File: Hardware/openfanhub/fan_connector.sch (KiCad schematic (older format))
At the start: 10 parts, among them M1 Fan_4pin, Q4 Q_PMOS_DGS, Q5 Q_NMOS_DGS, Q6 Q_NMOS_DGS

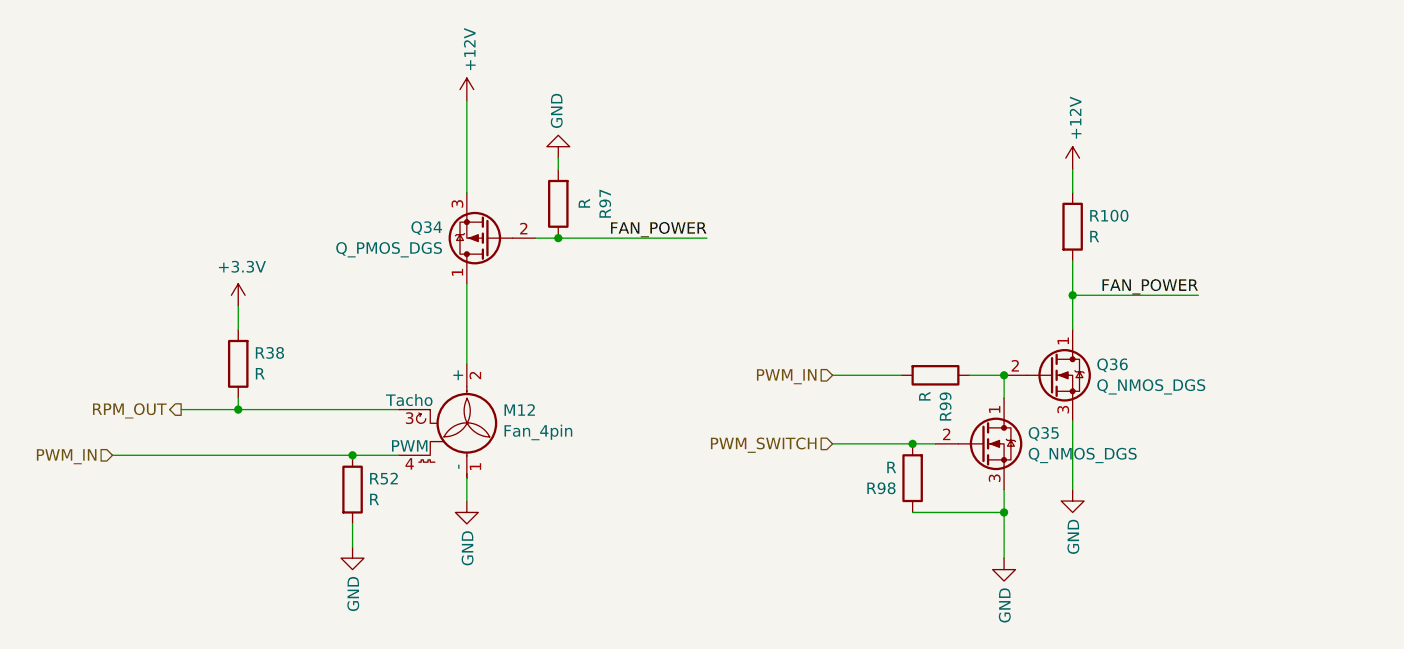
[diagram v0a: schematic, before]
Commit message: Idea to enable 3 pin PWM support with minimal components
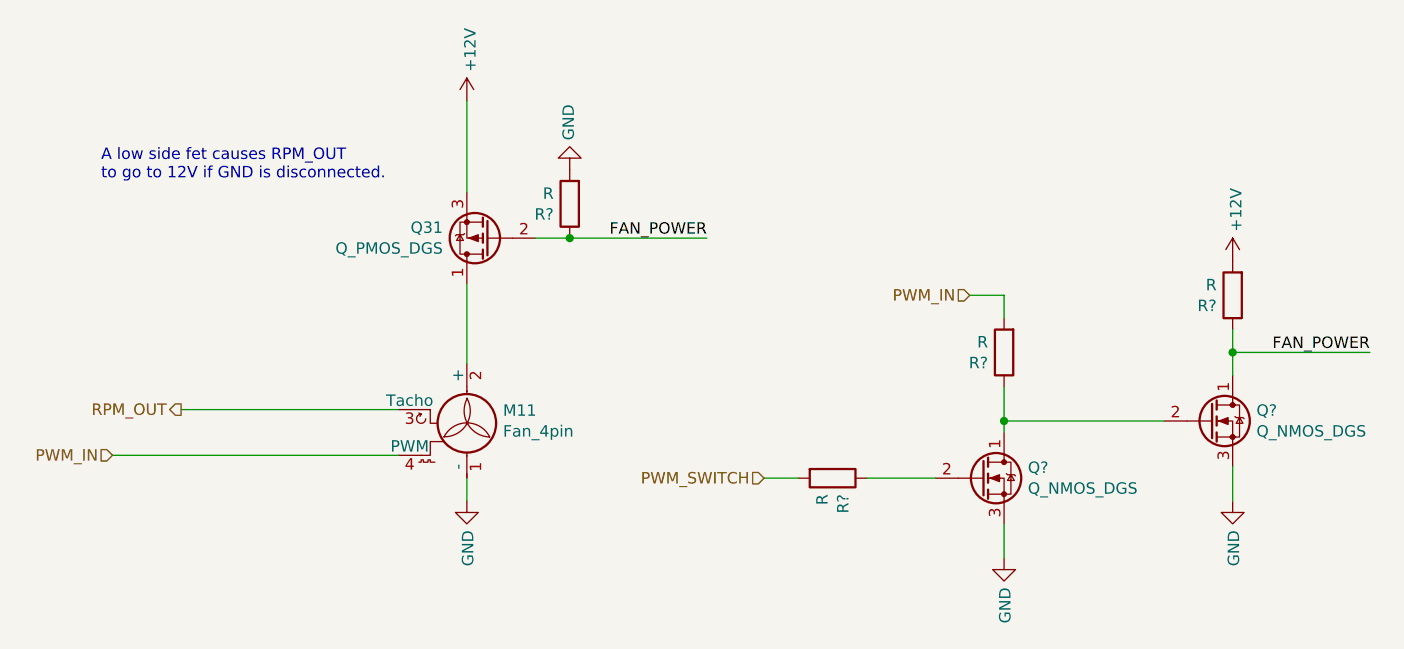
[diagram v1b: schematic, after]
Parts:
- removed Q5, Q6: Q_NMOS_DGS, symbol Device:Q_NMOS_DGS
- removed R41, R5, R53, R54, R55, R56: R, symbol Device:R
- added Q? (x2): Q_NMOS_DGS, symbol Device:Q_NMOS_DGS
- added R? (x4): R, symbol Device:R
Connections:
- net +12V: now also R?.2
- net FAN_POWER: now also Q?.1 (D), R?.1, R?.1
- net GND: now also Q?.3 (S), Q?.3 (S), R?.2
- net PWM_IN: now also R?.2
- net PWM_SWITCH: now also R?.2
- new net: Q?.1 (D), Q?.2 (G), R?.1
- new net: Q?.2 (G), R?.1
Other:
- note added: "A low side fet causes RPM_OUT \nto go to 12V if GND is disconnected."
